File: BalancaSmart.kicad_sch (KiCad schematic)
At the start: 49 parts, among them J1 Load Cell, Q3 NMOS, Q4 S8050, Q5 IRF7309PBF, SW1 SW_Push, U1 HX711-Mod, U2 ADS1115-module, U3 HX-2S-JH20, U4 XL4015

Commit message: alterações no circuito
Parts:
- removed C1: 1uF, Capacitor_THT:C_Disc_D5.0mm_W2.5mm_P2.50mm, symbol Device:C
- removed C2: 0.1uF, Capacitor_THT:C_Disc_D5.0mm_W2.5mm_P2.50mm, symbol Device:C
- removed C3: 10uF, Capacitor_THT:C_Disc_D5.0mm_W2.5mm_P2.50mm, symbol Device:C
- removed C4: 10uF, Capacitor_THT:C_Radial_D6.3mm_H7.0mm_P2.50mm, symbol Device:C
- removed D1, D2, D3, D4, D5, D6, D7, D8, D9: LED, Connector_PinHeader_2.54mm:PinHeader_1x02_P2.54mm_Vertical, symbol Device:LED
- removed D11: 1N5400, Diode_THT:D_DO-201AD_P15.24mm_Horizontal, symbol Diode:1N5400
- removed JP1: Jumper_2_Bridged, Resistor_THT:R_Axial_DIN0204_L3.6mm_D1.6mm_P7.62mm_Horizontal, symbol Jumper:Jumper_2_Bridged
- removed Q3: NMOS, Package_TO_SOT_THT:TO-220-3_Vertical, symbol Simulation_SPICE:NMOS
- removed Q5: IRF7309PBF, Package_SO:SOIC-8_3.9x4.9mm_P1.27mm, symbol Transistor_FET:IRF7309PBF
- removed R10, R11, R12, R13, R14, R7, R8, R9: 100, Resistor_THT:R_Axial_DIN0204_L3.6mm_D1.6mm_P7.62mm_Horizontal, symbol Device:R
- removed R15: 1k, Resistor_THT:R_Axial_DIN0204_L3.6mm_D1.6mm_P7.62mm_Horizontal, symbol Device:R
- added J2: NeoPixel Ring Light, symbol Connector:Screw_Terminal_01x03
- added Q1: IRF9540N, Package_TO_SOT_THT:TO-220-3_Vertical, symbol Transistor_FET:IRF9540N
- added U5: Optocoupler_DC_PhotoNPN_AKEC, symbol Isolator:Optocoupler_DC_PhotoNPN_AKEC
- BT1, SW1: footprint TerminalBlock:TerminalBlock_MaiXu_MX126-5.0-02P_1x02_P5.00mm -> (none)
- R1: value 10k -> 1M; footprint Resistor_THT:R_Axial_DIN0204_L3.6mm_D1.6mm_P7.62mm_Horizontal -> (none)
- R2: footprint Resistor_THT:R_Axial_DIN0204_L3.6mm_D1.6mm_P7.62mm_Horizontal -> (none)
- R3: value 100k -> 1k; footprint Resistor_THT:R_Axial_DIN0204_L3.6mm_D1.6mm_P7.62mm_Horizontal -> (none)
- R4: value 300k -> 1k; footprint Resistor_THT:R_Axial_DIN0204_L3.6mm_D1.6mm_P7.62mm_Horizontal -> (none)
- R5: value 1k -> 2k; footprint Resistor_THT:R_Axial_DIN0204_L3.6mm_D1.6mm_P7.62mm_Horizontal -> (none)
- R6: value 100 -> 1k; footprint Resistor_THT:R_Axial_DIN0204_L3.6mm_D1.6mm_P7.62mm_Horizontal -> (none)
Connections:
- net GND is gone; now on net Earth: C7.2, C8.2, SW1.1, U4.4 (Pin_4)
- net +5V: now also R3.1, Q1.2 (D); no longer R2.1, R6.2
- net Earth: now also R5.2, J2.1 (Pin_1), U5.2, U5.3
- net Sinal de desligamento: now also R4.2
- net pino 5v rasp: now also A1.4 (+5V), J2.2 (Pin_2), Q1.3 (S); no longer R3.2
- net at SW1.2: now also R2.2, R3.2, R4.1; no longer R1.2
- net Ring Light: now reaches A1.11 (GP17)
- net Ring Light: now also J2.3 (Pin_3)
- net button pin: now reaches A1.35 (GP19)
- net button pin: now also R6.2
- net at R6.1: now also U5.4
- new net: Q1.1 (G), R1.2, R2.1, U5.1
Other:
- note added: "On/Off push button"
- note removed: "AUTO-OFF"
- note removed: "Controle de energia com latch eletrônico"
- note removed: "LEDS para iluminação do alimento"
- moved on the sheet: J1, U1

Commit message: organização do esquemático
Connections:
- net +5V: no longer BZ1.1 (+)
- net pino 5v rasp: now also BZ1.1 (+)
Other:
- note added: "Iluminação"
- moved on the sheet: A1, BT1, BZ1, C7, C8, C9, J1, J2, Q1, Q4, R1, R18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

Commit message: trilhas
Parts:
- J2: footprint (none) -> TerminalBlock:TerminalBlock_MaiXu_MX126-5.0-03P_1x03_P5.00mm
- R1, R2, R3, R4, R5, R6: footprint (none) -> Resistor_THT:R_Axial_DIN0204_L3.6mm_D1.6mm_P7.62mm_Horizontal
- SW1: footprint (none) -> TerminalBlock:TerminalBlock_MaiXu_MX126-5.0-02P_1x02_P5.00mm
- U3: footprint TerminalBlock:TerminalBlock_MaiXu_MX126-5.0-04P_1x04_P5.00mm -> TerminalBlock:TerminalBlock_MaiXu_MX126-5.0-02P_1x02_P5.00mm
- U5: footprint (none) -> Package_DIP:DIP-4_W7.62mm_Socket_LongPads
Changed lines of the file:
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@@
 			)
 		)
-		(property "Footprint" ""
+		(property "Footprint" "Resistor_THT:R_Axial_DIN0204_L3.6mm_D1.6mm_P7.62mm_Horizontal"
 			(at 35.052 147.32 90)
 			(hide yes)
@@
 			)
 		)
-		(property "Footprint" ""
+		(property "Footprint" "TerminalBlock:TerminalBlock_MaiXu_MX126-5.0-03P_1x03_P5.00mm"
 			(at 217.17 92.71 0)
 			(hide yes)
@@
 			)
 		)
-		(property "Footprint" "TerminalBlock:TerminalBlock_MaiXu_MX126-5.0-04P_1x04_P5.00mm"
+		(property "Footprint" "TerminalBlock:TerminalBlock_MaiXu_MX126-5.0-02P_1x02_P5.00mm"
 			(at 50.8 99.06 0)
 			(hide yes)
@@
 			)
 		)
-		(property "Footprint" ""
+		(property "Footprint" "Resistor_THT:R_Axial_DIN0204_L3.6mm_D1.6mm_P7.62mm_Horizontal"
 			(at 61.722 157.48 90)
 			(hide yes)
@@
 			)
 		)
-		(property "Footprint" ""
+		(property "Footprint" "Resistor_THT:R_Axial_DIN0204_L3.6mm_D1.6mm_P7.62mm_Horizontal"
 			(at 102.87 141.478 90)
 			(hide yes)
@@
 			)
 		)
-		(property "Footprint" ""
+		(property "Footprint" "Resistor_THT:R_Axial_DIN0204_L3.6mm_D1.6mm_P7.62mm_Horizontal"
 			(at 40.132 135.89 90)
 			(hide yes)
@@
 			)
 		)
-		(property "Footprint" ""
+		(property "Footprint" "TerminalBlock:TerminalBlock_MaiXu_MX126-5.0-02P_1x02_P5.00mm"
 			(at 45.72 160.02 0)
 			(hide yes)
@@
 			)
 		)
-		(property "Footprint" ""
+		(property "Footprint" "Resistor_THT:R_Axial_DIN0204_L3.6mm_D1.6mm_P7.62mm_Horizontal"
 			(at 49.022 147.32 90)
 			(hide yes)
@@
 			)
 		)
-		(property "Footprint" ""
+		(property "Footprint" "Resistor_THT:R_Axial_DIN0204_L3.6mm_D1.6mm_P7.62mm_Horizontal"
 			(at 61.722 166.37 90)
 			(hide yes)
@@
 			)
 		)
-		(property "Footprint" ""
+		(property "Footprint" "Package_DIP:DIP-4_W7.62mm_Socket_LongPads"
 			(at 78.74 147.32 0)
 			(hide yes)

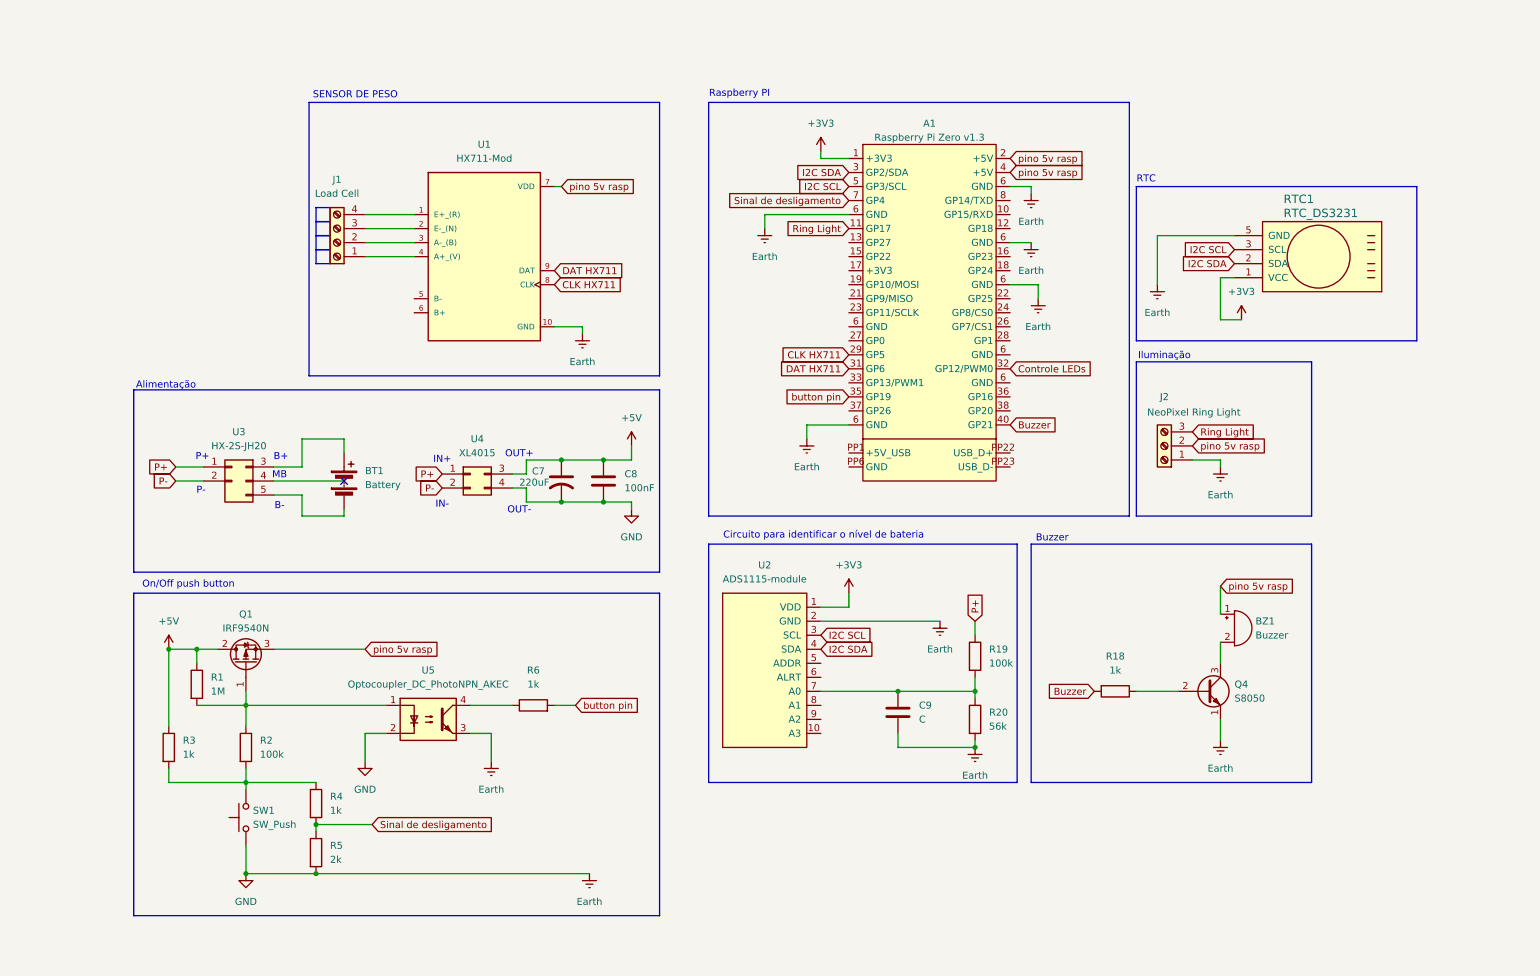
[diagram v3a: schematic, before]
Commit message: alteração no circuito de liga/desliga
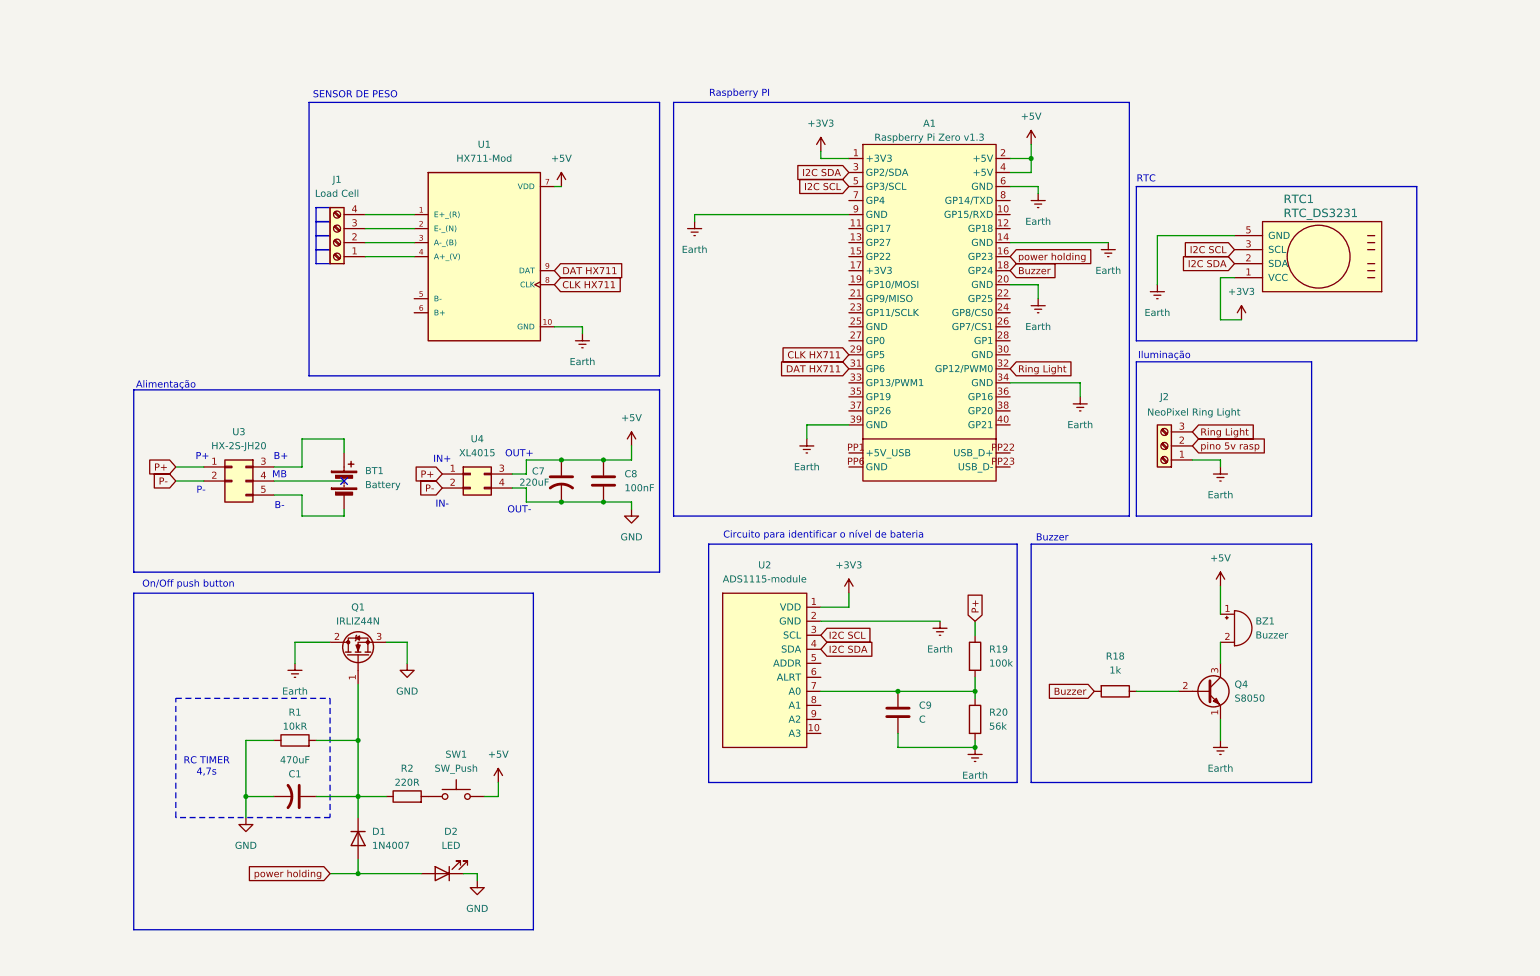
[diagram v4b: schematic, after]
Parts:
- removed Q1: IRF9540N, Package_TO_SOT_THT:TO-220-3_Vertical, symbol Transistor_FET:IRF9540N
- removed R3, R4, R6: 1k, Resistor_THT:R_Axial_DIN0204_L3.6mm_D1.6mm_P7.62mm_Horizontal, symbol Device:R
- removed R5: 2k, Resistor_THT:R_Axial_DIN0204_L3.6mm_D1.6mm_P7.62mm_Horizontal, symbol Device:R
- removed U5: Optocoupler_DC_PhotoNPN_AKEC, Package_DIP:DIP-4_W7.62mm_Socket_LongPads, symbol Isolator:Optocoupler_DC_PhotoNPN_AKEC
- added C1: 470uF, Capacitor_THT:C_Radial_D6.3mm_H7.0mm_P2.50mm, symbol Device:C_US
- added D1: 1N4007, Diode_THT:D_DO-41_SOD81_P10.16mm_Horizontal, symbol Diode:1N4007
- added D2: LED, LED_THT:LED_D5.0mm, symbol Device:LED
- added Q1: IRLIZ44N, Package_TO_SOT_THT:TO-220F-3_Vertical, symbol Transistor_FET:IRLIZ44N
- R1: value 1M -> 10kR
- R2: value 100k -> 220R
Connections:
- net Controle LEDs is gone; now on net Ring Light: A1.32 (GP12/PWM0)
- net +5V: now also A1.2 (+5V), A1.4 (+5V), BZ1.1 (+), SW1.2, U1.7 (VDD); no longer R1.1
- net Buzzer: now also A1.18 (GP24); no longer A1.40 (GP21)
- net Earth: now also A1.14 (GND), A1.20 (GND), A1.34 (GND), A1.39 (GND), A1.9 (GND), Q1.2 (D); no longer C7.2, C8.2, SW1.1, U4.4 (Pin_4)
- net Ring Light: no longer A1.11 (GP17)
- net pino 5v rasp: no longer A1.2 (+5V), A1.4 (+5V), BZ1.1 (+), U1.7 (VDD)
- net at R2.2: now also SW1.1; no longer SW1.2
- net at R1.2, R2.1: now also C1.1, D1.1 (K), Q1.1 (G)
- net power holding: now reaches A1.16 (GP23)
- net power holding: now also D1.2 (A), D2.2 (A)
- net Sinal de desligamento: no longer names the net of A1.7 (GP4)
- net button pin: no longer names the net of A1.35 (GP19)
- new net GND: C1.2, C7.2, C8.2, D2.1 (K), Q1.3 (S), R1.1, U4.4 (Pin_4)
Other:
- note added: "RC TIMER 4,7s"

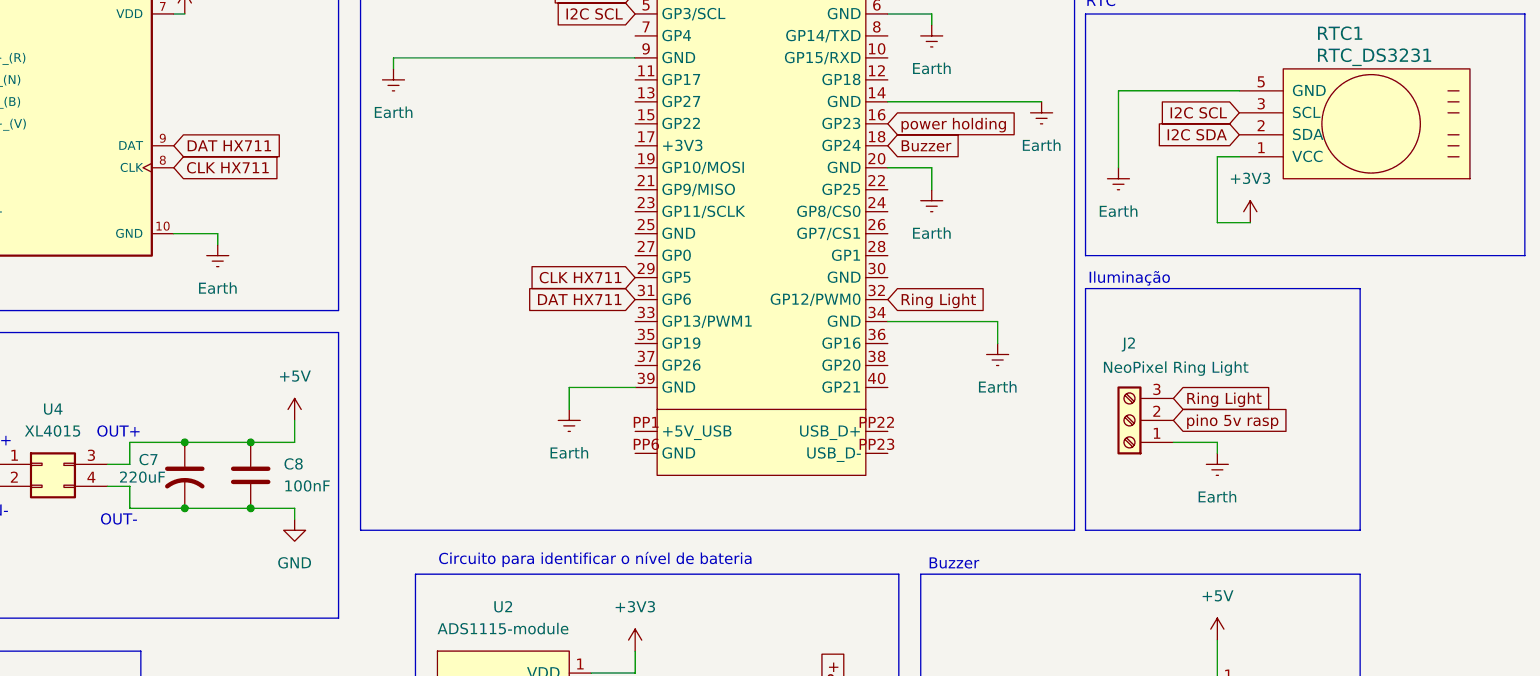
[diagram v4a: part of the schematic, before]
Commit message: adicionado resistor para a ring light e refeitas as rotas (tudo roteado corretamente)
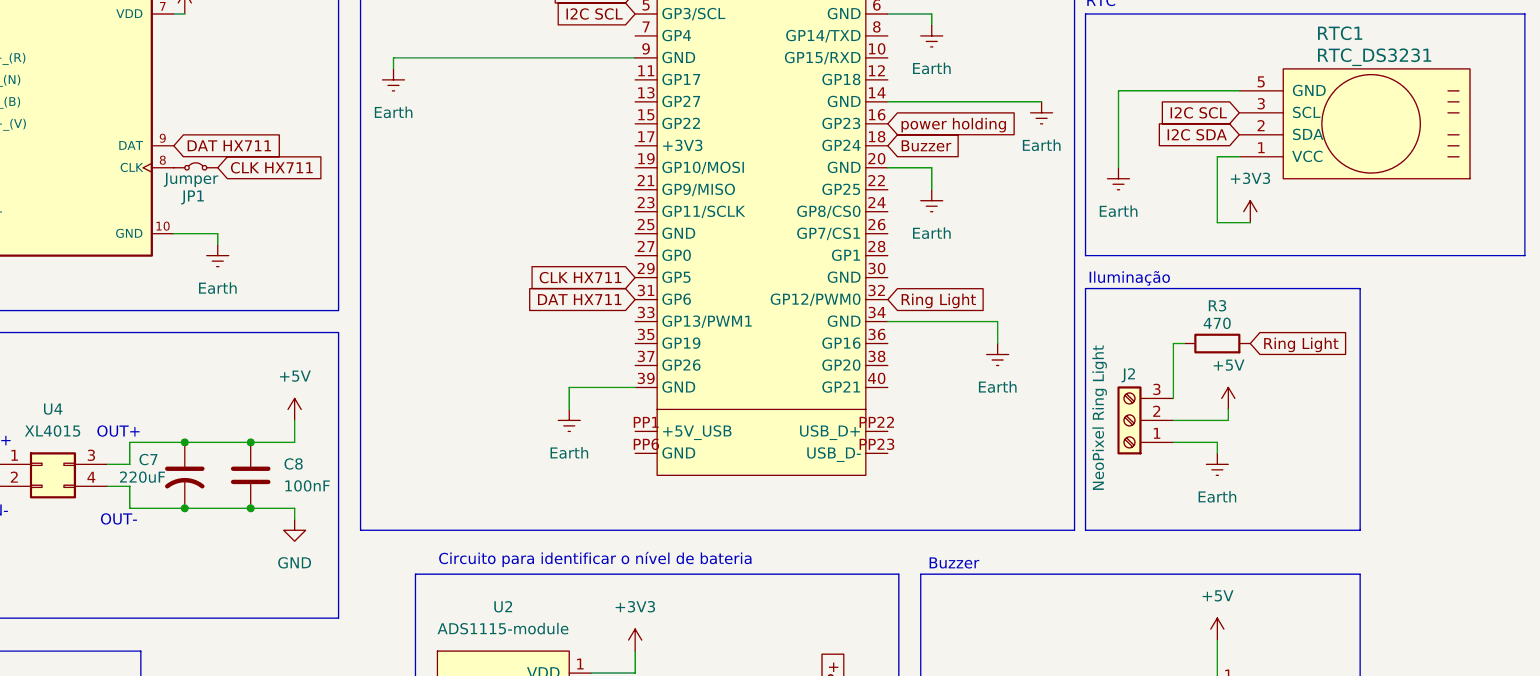
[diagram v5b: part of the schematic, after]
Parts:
- added JP1: Jumper, Resistor_THT:R_Axial_DIN0207_L6.3mm_D2.5mm_P10.16mm_Horizontal, symbol Jumper:Jumper_2_Small_Bridged
- added R3: 470, Resistor_THT:R_Axial_DIN0204_L3.6mm_D1.6mm_P7.62mm_Horizontal, symbol Device:R
- Q4: footprint Package_TO_SOT_THT:TO-92_Inline -> Connector_PinHeader_2.54mm:PinHeader_1x03_P2.54mm_Vertical
- R18, R2: footprint Resistor_THT:R_Axial_DIN0204_L3.6mm_D1.6mm_P7.62mm_Horizontal -> Resistor_THT:R_Axial_DIN0207_L6.3mm_D2.5mm_P10.16mm_Horizontal
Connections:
- net pino 5v rasp is gone; now on net +5V: J2.2 (Pin_2)
- net CLK HX711: now also JP1.2 (B); no longer U1.8 (CLK)
- net Ring Light: now also R3.2; no longer J2.3 (Pin_3)
- new net: J2.3 (Pin_3), R3.1
- new net: JP1.1 (A), U1.8 (CLK)

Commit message: adiciona borne para o display
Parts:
- added J3: Display, TerminalBlock:TerminalBlock_MaiXu_MX126-5.0-02P_1x02_P5.00mm, symbol Connector:Screw_Terminal_01x02
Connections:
- net +5V: now also J3.2 (Pin_2)
- net Earth: now also J3.1 (Pin_1)
